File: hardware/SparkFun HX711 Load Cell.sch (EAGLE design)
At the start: 25 parts, among them Q1 MMBT4403, U1 HX711

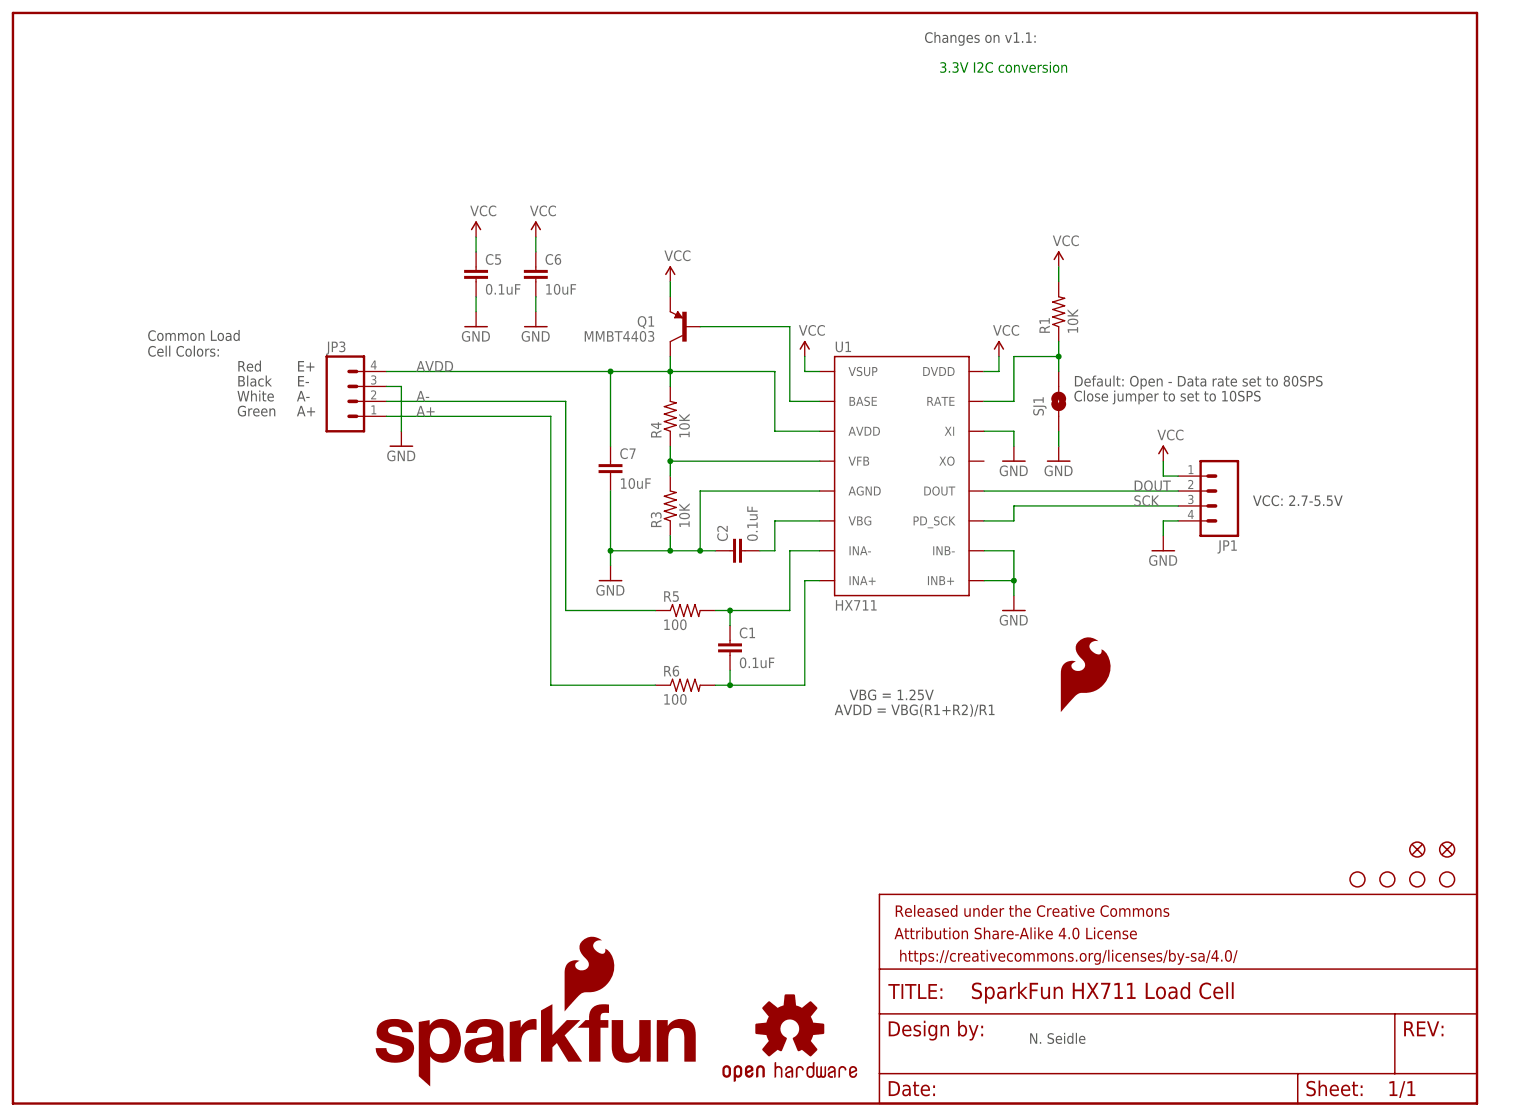
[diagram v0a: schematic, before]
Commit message: Changes from initial QC checklist. Adding datasheet.
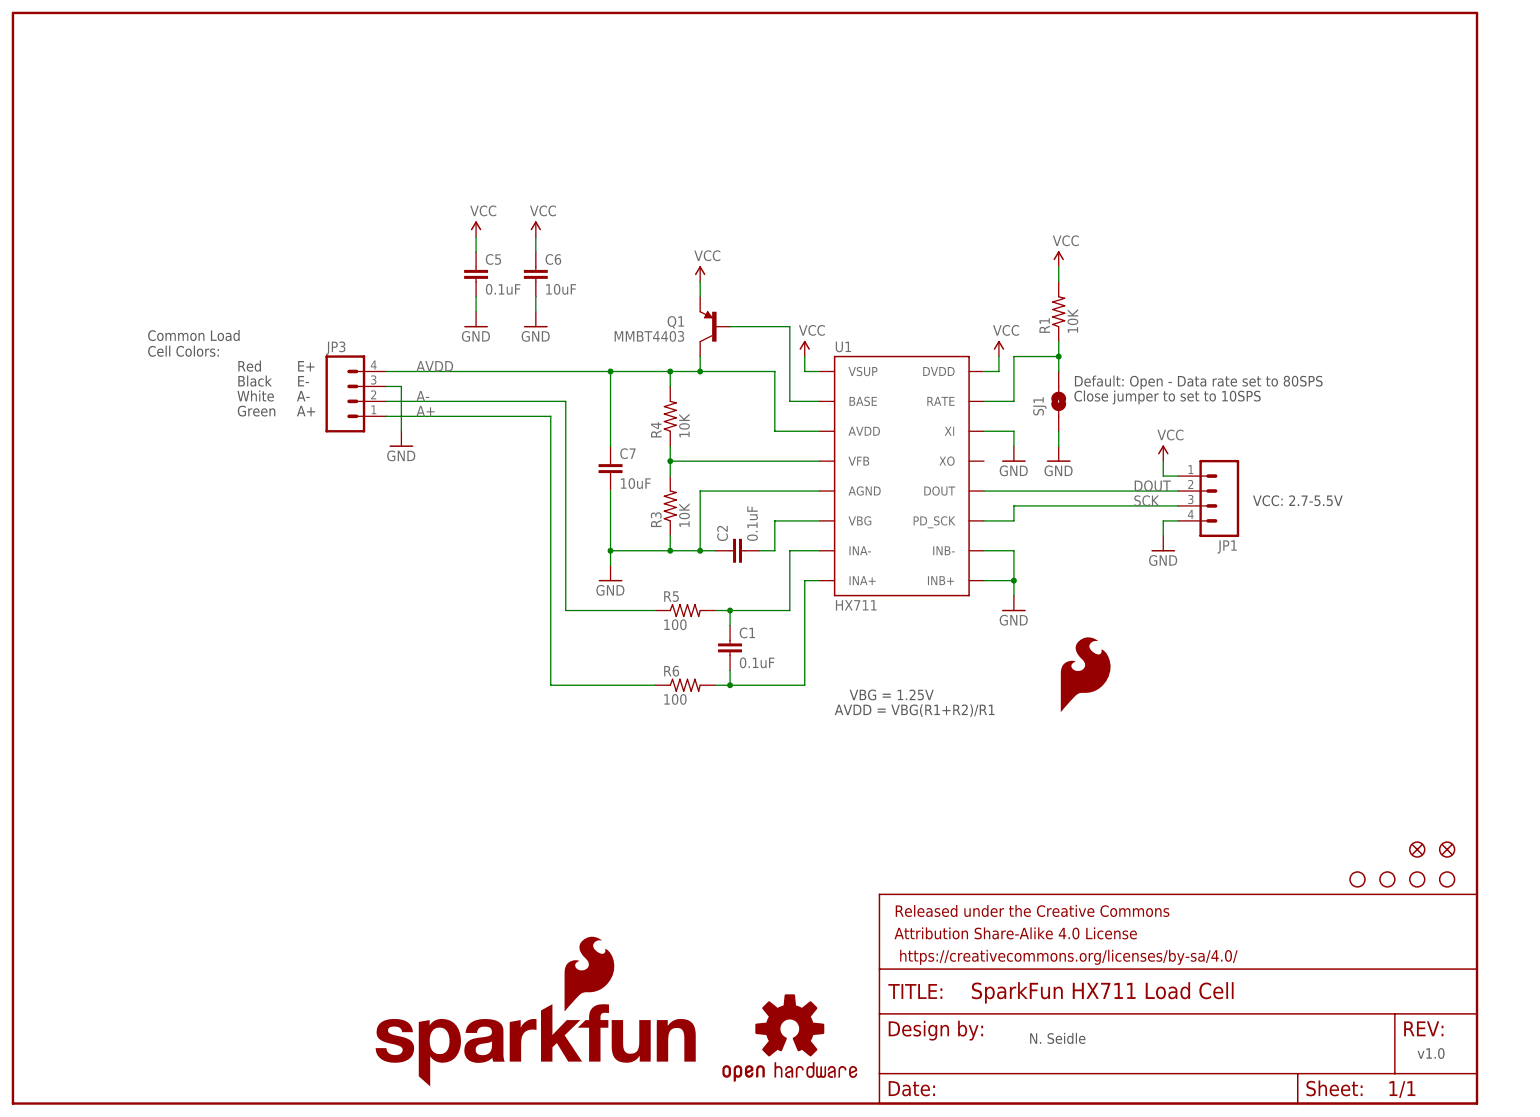
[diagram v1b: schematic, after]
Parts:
- U1: device HX711:HX711 -> Testing:HX711HX711
- renumbered U$7 to U7
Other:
- note added: "v1.0"
- note removed: "3.3V I2C conversion"
- note removed: "Changes on v1.1:"
- moved on the sheet: Q1

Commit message: Spread out 0603 components and fixed silk. See issue 1.
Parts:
- removed R6: 100, SparkFun-Resistors:100OHM1/10W1%(0603)
- added R2: 10K, SparkFun-Resistors:10KOHM1/10W1%(0603)0603
- R3, R4: value 10K -> 100; device SparkFun-Resistors:10KOHM1/10W1%(0603)0603 -> SparkFun-Resistors:100OHM1/10W1%(0603)
- R5: value 100 -> 10K; device SparkFun-Resistors:100OHM1/10W1%(0603) -> SparkFun-Resistors:10KOHM1/10W1%(0603)0603
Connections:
- net DOUT renamed DAT
- net A+: now also R4.1; no longer R6.1
- net A-: now also R3.1; no longer R5.1
- net AVDD: now also R1.2; no longer R4.2
- net GND: now also R2.1; no longer R3.1
- net N$1: now also R5.1; no longer R1.1
- net N$2: now also R3.2; no longer R5.2
- net N$3: now also R4.2; no longer R6.2
- net N$6: now also R1.1, R2.2; no longer R3.2, R4.1
- net VCC: now also R5.2; no longer R1.2
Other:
- note added: "IO: 2.7-5.5V"
- note added: "v01"
- note removed: "v1.0"
- moved on the sheet: C5, C6, R1, R3, R4, R5
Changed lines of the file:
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@@
 <part name="Q1" library="SparkFun-DiscreteSemi" deviceset="TRANSISTOR_PNP" device="MMBT4403" value="MMBT4403"/>
 <part name="GND1" library="SparkFun-Aesthetics" deviceset="GND" device=""/>
-<part name="R5" library="SparkFun-Resistors" deviceset="100OHM1/10W1%(0603)" device="" value="100"/>
-<part name="R6" library="SparkFun-Resistors" deviceset="100OHM1/10W1%(0603)" device="" value="100"/>
+<part name="R3" library="SparkFun-Resistors" deviceset="100OHM1/10W1%(0603)" device="" value="100"/>
+<part name="R4" library="SparkFun-Resistors" deviceset="100OHM1/10W1%(0603)" device="" value="100"/>
 <part name="C6" library="SparkFun-Capacitors" deviceset="10UF50V20%(1210)" device="" value="10uF"/>
 <part name="C7" library="SparkFun-Capacitors" deviceset="10UF50V20%(1210)" device="" value="10uF"/>
@@
 <part name="SUPPLY1" library="SparkFun-Aesthetics" deviceset="VCC" device=""/>
 <part name="GND4" library="SparkFun-Aesthetics" deviceset="GND" device=""/>
-<part name="R3" library="SparkFun-Resistors" deviceset="10KOHM1/10W1%(0603)" device="0603" value="10K"/>
-<part name="R4" library="SparkFun-Resistors" deviceset="10KOHM1/10W1%(0603)" device="0603" value="10K"/>
+<part name="R2" library="SparkFun-Resistors" deviceset="10KOHM1/10W1%(0603)" device="0603" value="10K"/>
+<part name="R1" library="SparkFun-Resistors" deviceset="10KOHM1/10W1%(0603)" device="0603" value="10K"/>
 <part name="GND5" library="SparkFun-Aesthetics" deviceset="GND" device=""/>
 <part name="JP3" library="SparkFun-Connectors" deviceset="M04" device="PTH"/>
 <part name="GND6" library="SparkFun-Aesthetics" deviceset="GND" device=""/>
 <part name="SUPPLY5" library="SparkFun-Aesthetics" deviceset="VCC" device=""/>
-<part name="R1" library="SparkFun-Resistors" deviceset="10KOHM1/10W1%(0603)" device="0603" value="10K"/>
+<part name="R5" library="SparkFun-Resistors" deviceset="10KOHM1/10W1%(0603)" device="0603" value="10K"/>
 <part name="SUPPLY6" library="SparkFun-Aesthetics" deviceset="VCC" device=""/>
 <part name="SJ1" library="SparkFun-Passives" deviceset="JUMPER-PAD-2-NO" device="YES_SILK" value=""/>
@@
 <plain>
 <text x="210.82" y="101.6" size="1.778" layer="97">VCC: 2.7-5.5V</text>
-<text x="142.24" y="68.58" size="1.778" layer="97">VBG = 1.25V</text>
-<text x="139.7" y="66.04" size="1.778" layer="97">AVDD = VBG(R1+R2)/R1</text>
+<text x="121.158" y="135.382" size="1.778" layer="97">VBG = 1.25V</text>
+<text x="64.262" y="129.286" size="1.778" layer="97">AVDD = VBG(R1+R2)/R1</text>
 <text x="180.34" y="121.92" size="1.778" layer="97">Default: Open - Data rate set to 80SPS</text>
 <text x="180.34" y="119.38" size="1.778" layer="97">Close jumper to set to 10SPS</text>
@@
 <text x="22.86" y="127" size="1.778" layer="97">Common Load
 Cell Colors:</text>
-<text x="172.72" y="10.16" size="1.778" layer="97">N. Seidle</text>
-<text x="238.76" y="7.62" size="1.778" layer="97">v1.0</text>
+<text x="172.72" y="10.16" size="1.778" layer="94">N. Seidle</text>
+<text x="238.76" y="7.62" size="1.778" layer="94">v01</text>
+<text x="210.82" y="99.06" size="1.778" layer="97">IO: 2.7-5.5V</text>
 </plain>
 <instances>
@@
 <instance part="Q1" gate="G$1" x="119.38" y="132.08" rot="MR0"/>
 <instance part="GND1" gate="1" x="195.58" y="93.98"/>
-<instance part="R5" gate="G$1" x="114.3" y="83.82"/>
-<instance part="R6" gate="G$1" x="114.3" y="71.12"/>
-<instance part="C6" gate="G$1" x="88.9" y="139.7"/>
+<instance part="R3" gate="G$1" x="114.3" y="83.82"/>
+<instance part="R4" gate="G$1" x="114.3" y="71.12"/>
+<instance part="C6" gate="G$1" x="104.14" y="144.78"/>
 <instance part="C7" gate="G$1" x="101.6" y="106.68"/>
 <instance part="GND2" gate="1" x="170.18" y="109.22"/>
-<instance part="SUPPLY2" gate="G$1" x="88.9" y="147.32"/>
-<instance part="GND3" gate="1" x="88.9" y="132.08"/>
+<instance part="SUPPLY2" gate="G$1" x="104.14" y="152.4"/>
+<instance part="GND3" gate="1" x="104.14" y="137.16"/>
 <instance part="SUPPLY3" gate="G$1" x="134.62" y="127"/>
 <instance part="SUPPLY4" gate="G$1" x="167.64" y="127"/>
 <instance part="SUPPLY1" gate="G$1" x="116.84" y="139.7"/>
 <instance part="GND4" gate="1" x="66.04" y="111.76"/>
-<instance part="R3" gate="G$1" x="111.76" y="101.6" rot="R90"/>
-<instance part="R4" gate="G$1" x="111.76" y="116.84" rot="R90"/>
+<instance part="R2" gate="G$1" x="111.76" y="101.6" rot="R90"/>
+<instance part="R1" gate="G$1" x="111.76" y="116.84" rot="R90"/>
 <instance part="GND5" gate="1" x="101.6" y="88.9"/>
 <instance part="JP3" gate="G$1" x="58.42" y="119.38"/>
 <instance part="GND6" gate="1" x="170.18" y="83.82"/>
 <instance part="SUPPLY5" gate="G$1" x="195.58" y="109.22"/>
-<instance part="R1" gate="G$1" x="177.8" y="134.62" rot="R90"/>
+<instance part="R5" gate="G$1" x="177.8" y="134.62" rot="R90"/>
 <instance part="SUPPLY6" gate="G$1" x="177.8" y="142.24"/>
 <instance part="SJ1" gate="G$1" x="177.8" y="119.38" rot="R90"/>
 <instance part="GND7" gate="1" x="177.8" y="109.22"/>
 <instance part="C1" gate="G$1" x="121.92" y="76.2"/>
-<instance part="C5" gate="G$1" x="78.74" y="139.7"/>
+<instance part="C5" gate="G$1" x="93.98" y="144.78"/>
 <instance part="C2" gate="G$1" x="124.46" y="93.98" rot="R90"/>
-<instance part="SUPPLY7" gate="G$1" x="78.74" y="147.32"/>
-<instance part="GND8" gate="1" x="78.74" y="132.08"/>
+<instance part="SUPPLY7" gate="G$1" x="93.98" y="152.4"/>
+<instance part="GND8" gate="1" x="93.98" y="137.16"/>
 <instance part="LOGO3" gate="G$1" x="177.8" y="66.04"/>
 <instance part="FID1" gate="G$1" x="243.84" y="43.18"/>
@@
 <pinref part="C6" gate="G$1" pin="2"/>
 <pinref part="GND3" gate="1" pin="GND"/>
-<wire x1="88.9" y1="137.16" x2="88.9" y2="134.62" width="0.1524" layer="91"/>
+<wire x1="104.14" y1="142.24" x2="104.14" y2="139.7" width="0.1524" layer="91"/>
 </segment>
 <segment>
@@
 <wire x1="119.38" y1="93.98" x2="116.84" y2="93.98" width="0.1524" layer="91"/>
 <junction x="116.84" y="93.98"/>
-<pinref part="R3" gate="G$1" pin="1"/>
+<pinref part="R2" gate="G$1" pin="1"/>
 <pinref part="GND5" gate="1" pin="GND"/>
 <wire x1="101.6" y1="93.98" x2="101.6" y2="91.44" width="0.1524" layer="91"/>
@@
 <pinref part="C5" gate="G$1" pin="2"/>
 <pinref part="GND8" gate="1" pin="GND"/>
-<wire x1="78.74" y1="134.62" x2="78.74" y2="137.16" width="0.1524" layer="91"/>
+<wire x1="93.98" y1="139.7" x2="93.98" y2="142.24" width="0.1524" layer="91"/>
 </segment>
 </net>
@@
 <pinref part="C6" gate="G$1" pin="1"/>
 <pinref part="SUPPLY2" gate="G$1" pin="VCC"/>
-<wire x1="88.9" y1="144.78" x2="88.9" y2="147.32" width="0.1524" layer="91"/>
+<wire x1="104.14" y1="149.86" x2="104.14" y2="152.4" width="0.1524" layer="91"/>
 </segment>
 <segment>
@@
 </segment>
 <segment>
-<pinref part="R1" gate="G$1" pin="2"/>
+<pinref part="R5" gate="G$1" pin="2"/>
 <pinref part="SUPPLY6" gate="G$1" pin="VCC"/>
 <wire x1="177.8" y1="139.7" x2="177.8" y2="142.24" width="0.1524" layer="91"/>
@@
 <pinref part="C5" gate="G$1" pin="1"/>
 <pinref part="SUPPLY7" gate="G$1" pin="VCC"/>
-<wire x1="78.74" y1="147.32" x2="78.74" y2="144.78" width="0.1524" layer="91"/>
-</segment>
-</net>
-<net name="DOUT" class="0">
+<wire x1="93.98" y1="152.4" x2="93.98" y2="149.86" width="0.1524" layer="91"/>
+</segment>
+</net>
+<net name="DAT" class="0">
 <segment>
 <pinref part="U1" gate="U1" pin="DOUT"/>
@@
 <wire x1="137.16" y1="109.22" x2="111.76" y2="109.22" width="0.1524" layer="91"/>
 <junction x="111.76" y="109.22"/>
-<pinref part="R3" gate="G$1" pin="2"/>
-<pinref part="R4" gate="G$1" pin="1"/>
+<pinref part="R2" gate="G$1" pin="2"/>
+<pinref part="R1" gate="G$1" pin="1"/>
 </segment>
 </net>
@@
 <wire x1="129.54" y1="124.46" x2="116.84" y2="124.46" width="0.1524" layer="91"/>
 <junction x="101.6" y="124.46"/>
-<pinref part="R4" gate="G$1" pin="2"/>
+<pinref part="R1" gate="G$1" pin="2"/>
 <pinref part="JP3" gate="G$1" pin="4"/>
 <label x="68.58" y="124.46" size="1.778" layer="95"/>
@@
 <segment>
 <pinref part="U1" gate="U1" pin="RATE"/>
-<pinref part="R1" gate="G$1" pin="1"/>
+<pinref part="R5" gate="G$1" pin="1"/>
 <wire x1="165.1" y1="119.38" x2="170.18" y2="119.38" width="0.1524" layer="91"/>
 <pinref part="SJ1" gate="G$1" pin="2"/>
@@
 <wire x1="132.08" y1="93.98" x2="132.08" y2="83.82" width="0.1524" layer="91"/>
 <wire x1="132.08" y1="83.82" x2="121.92" y2="83.82" width="0.1524" layer="91"/>
-<pinref part="R5" gate="G$1" pin="2"/>
+<pinref part="R3" gate="G$1" pin="2"/>
 <pinref part="C1" gate="G$1" pin="1"/>
 <wire x1="121.92" y1="83.82" x2="119.38" y2="83.82" width="0.1524" layer="91"/>
@@
 <wire x1="134.62" y1="88.9" x2="134.62" y2="71.12" width="0.1524" layer="91"/>
 <wire x1="134.62" y1="71.12" x2="121.92" y2="71.12" width="0.1524" layer="91"/>
-<pinref part="R6" gate="G$1" pin="2"/>
+<pinref part="R4" gate="G$1" pin="2"/>
 <pinref part="C1" gate="G$1" pin="2"/>
 <wire x1="121.92" y1="71.12" x2="119.38" y2="71.12" width="0.1524" layer="91"/>
@@
 <wire x1="93.98" y1="119.38" x2="63.5" y2="119.38" width="0.1524" layer="91"/>
 <label x="68.58" y="119.38" size="1.778" layer="95"/>
-<pinref part="R5" gate="G$1" pin="1"/>
+<pinref part="R3" gate="G$1" pin="1"/>
 </segment>
 </net>
 <net name="A+" class="0">
 <segment>
-<pinref part="R6" gate="G$1" pin="1"/>
+<pinref part="R4" gate="G$1" pin="1"/>
 <wire x1="109.22" y1="71.12" x2="91.44" y2="71.12" width="0.1524" layer="91"/>
 <wire x1="91.44" y1="71.12" x2="91.44" y2="116.84" width="0.1524" layer="91"/>
